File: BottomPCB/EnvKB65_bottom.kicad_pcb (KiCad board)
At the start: 2 copper layers, 320.8 x 99.3 mm, 7 parts

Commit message: Generated some Gerbers and added some testing graphics for now.
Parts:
- removed Ref**: Val**, Logo:logo
- added G***: LOGO, Logo:patern, B.Cu at (224.8, 147.3)
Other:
- board text removed: "http://github.com/Envious-Data/Env-KB65M"

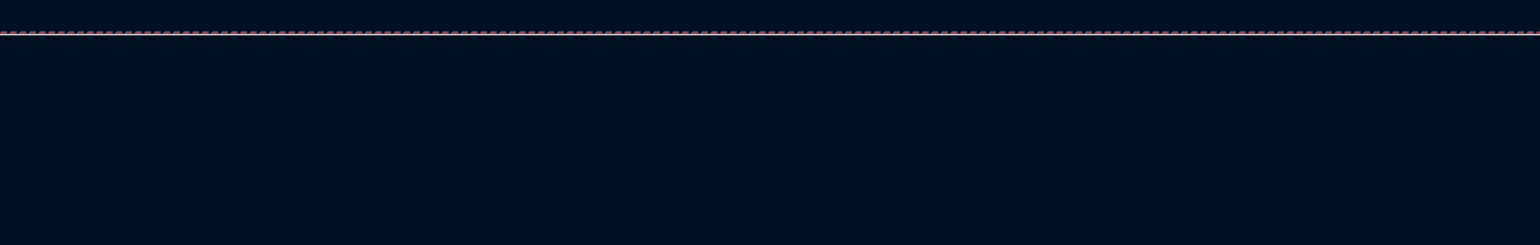
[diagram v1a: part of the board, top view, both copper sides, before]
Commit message: updated silkscreen and also made 32u switch plate.
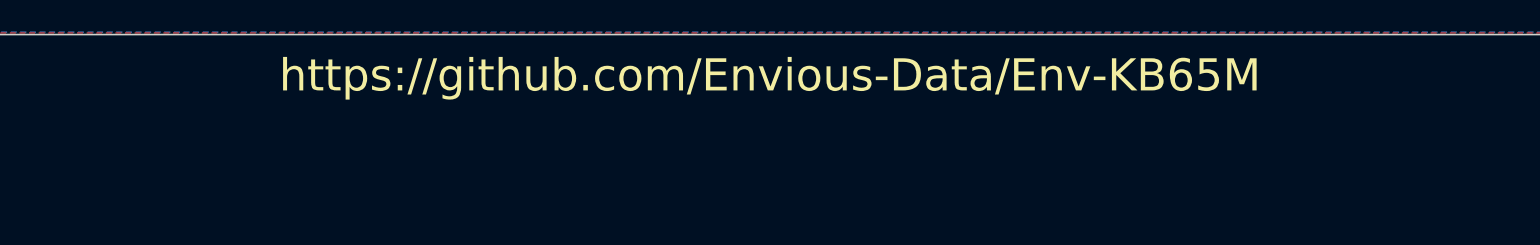
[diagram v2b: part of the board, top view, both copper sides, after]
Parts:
- G***: footprint Logo:patern -> Logo:topologylogoless
- moved G*** 0.09 mm to (224.9, 147.3)
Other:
- board text added: "https://github.com/Envious-Data/Env-KB65M"

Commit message: See List
* removed RP2040 and atmega32u4 versions
* updated main PCB to have larger holes
* fixed some stuff on the main PCB and added some labels
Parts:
- G***: footprint Logo:topologylogoless -> Logo:patern
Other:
- board text added: "Mechboards.co.uk"

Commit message: Removed Mechboards branding as there is now a mechboards fork
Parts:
- removed G***: LOGO, Logo:patern
- added kibuzzard-629270EE (x2): G***, kibuzzard-629270EE, B.Cu at (224.9, 147.3)
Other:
- net class Default removed
- board text removed: "Mechboards.co.uk"
